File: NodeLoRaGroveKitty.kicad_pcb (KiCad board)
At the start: 2 copper layers, 45 x 50 mm, 40 parts, among them P1 PICKIT PROGRAMMER, P2 Battery, P3 A0, P4 D9, P5 USB-Serial, P6 I2C, SW1 SW_BOOT, SW2 SW_RESET, U1 AP2112, U2 MCP73831T-2ATI/OT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

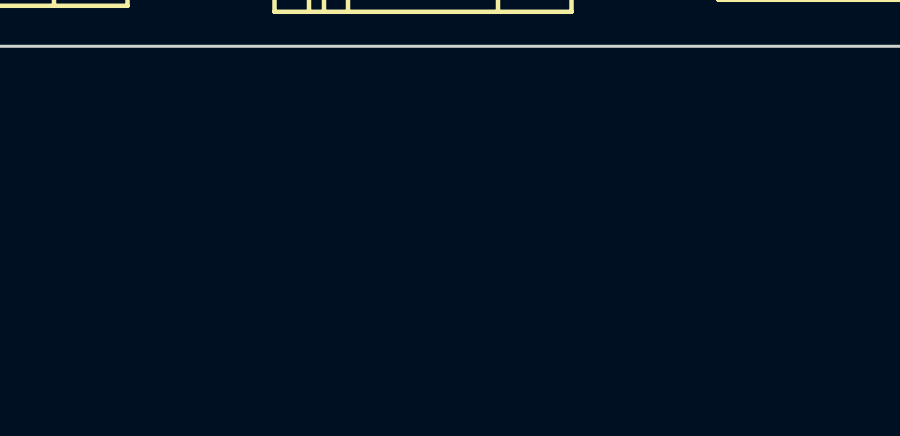
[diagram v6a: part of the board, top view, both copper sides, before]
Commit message: Add resistence and pin reset
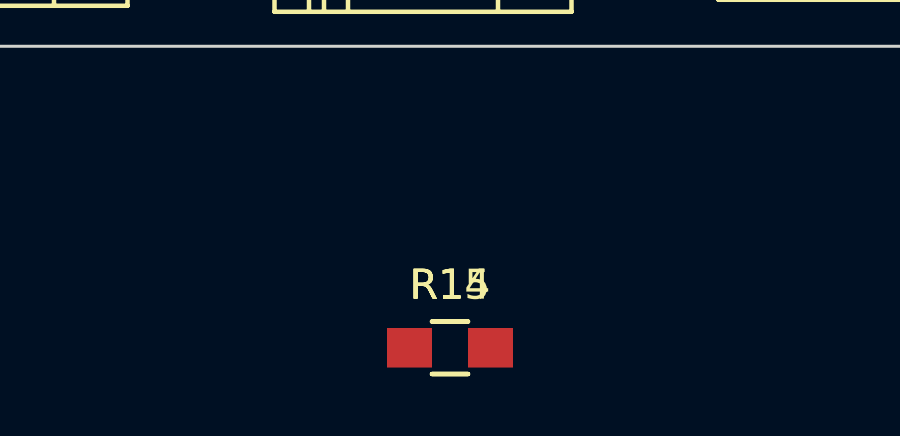
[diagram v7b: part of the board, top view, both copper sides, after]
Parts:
- added R14: 100K, Resistors_SMD:R_0805_HandSoldering, F.Cu at (124.5, 157.1)
- added R15: 10K, Resistors_SMD:R_0805_HandSoldering, F.Cu at (124.5, 157.1)
- R10: value 1K2 -> 100K
- R8: value 330R -> 100K
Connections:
- P3 pad 2: VCC -> +3V3
- P4 pad 2: VCC -> +3V3
- P4 pad 4: /GPIO15 -> /GPIO2
- P6 pad 2: VCC -> +3V3
- R10 pad 1: /A0 -> Net-(R10-Pad1)
- U3 pad 4: /GPIO16 -> /RST_RN
- U3 pad 5: /S_TX/GPIO14 -> /S_TX
- U3 pad 6: /S_RX/GPIO12 -> /S_RX
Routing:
- net VCC: track 136.8 -> 43.1 mm
- net Net-(MODULE1-Pad36): track 42.2 -> 95.3 mm
- net Net-(A1-Pad1): track 25.2 -> 45.5 mm
- net /GPIO2: track 0.00 -> 19.5 mm
- net /GPIO15: track 46.2 -> 26.7 mm
- net /A0: track 37.7 -> 19.4 mm
- net Net-(R10-Pad1): track 0.00 -> 18.3 mm
- net GND: track 68.8 -> 83.5 mm, vias 9 -> 10
- net /S_RX/GPIO12: track 22.6 -> 9.76 mm, vias 1 -> 0
- net /S_RX: track 0.00 -> 12.9 mm, vias 0 -> 1
- net /S_TX: track 0.00 -> 10.5 mm, vias 0 -> 1
- net /S_TX/GPIO14: track 16.2 -> 5.72 mm, vias 1 -> 0
- net +3V3: track 165.7 -> 171.4 mm, vias 3 -> 2

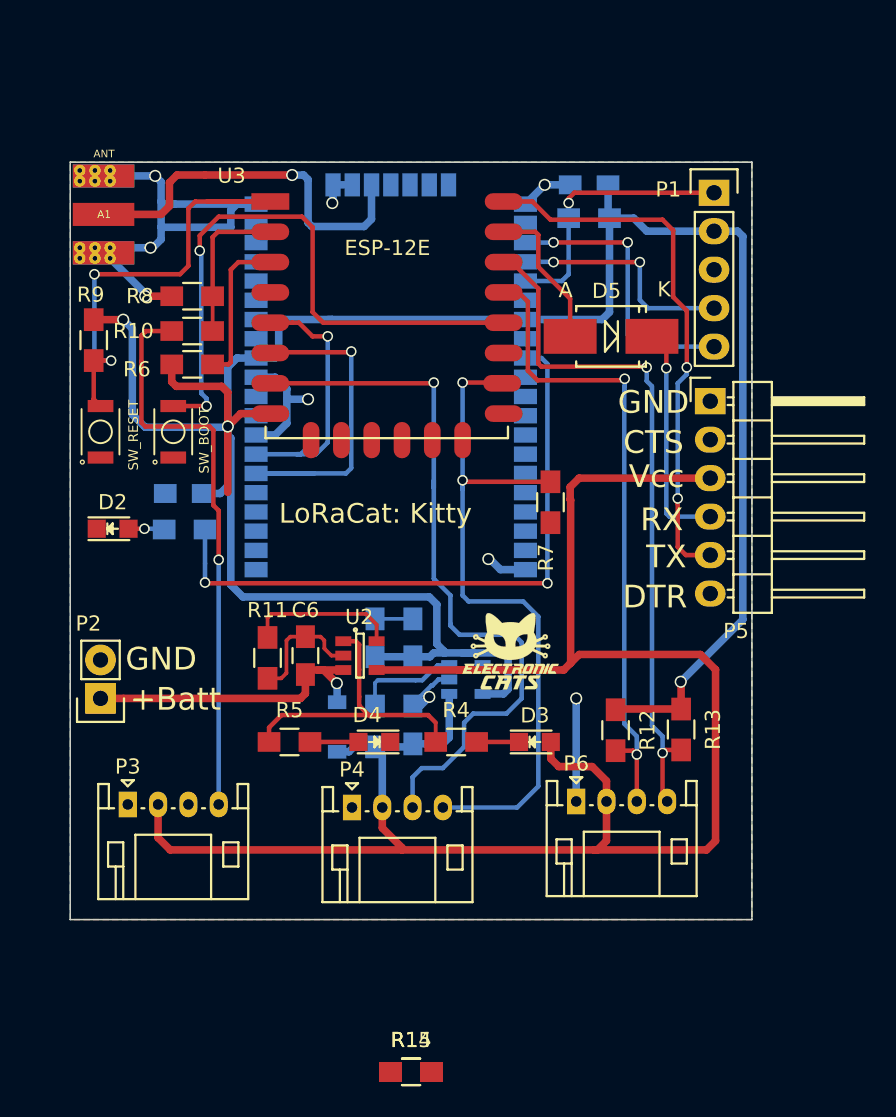
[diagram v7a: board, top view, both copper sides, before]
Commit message: Add res and rst pin PCB and Label's
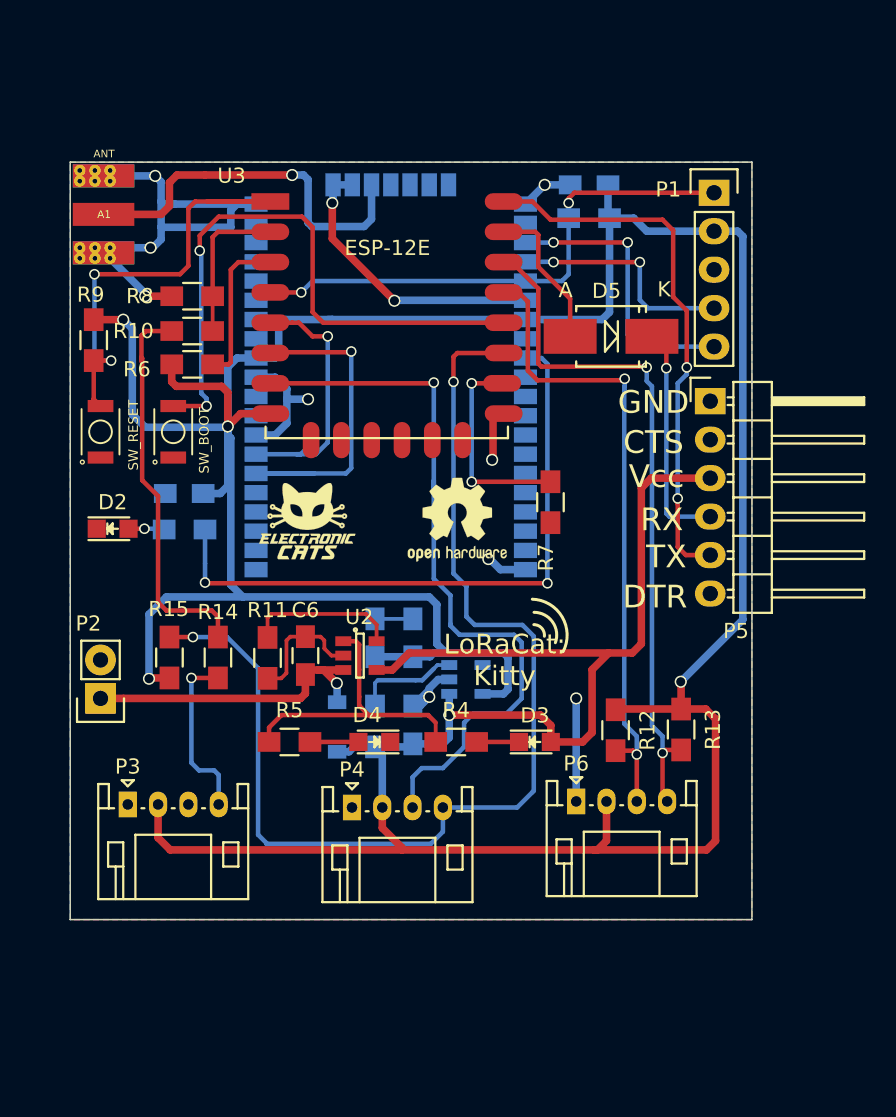
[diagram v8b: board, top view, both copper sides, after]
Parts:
- REF***: moved to F.Cu
- moved R15 31.7 mm to (108.5, 129.7), turned to 90 degrees
- moved R14 30.2 mm to (111.8, 129.7), turned to 90 degrees
- moved REF*** 21.8 mm to (135.0, 130.1)
- moved G*** 15.9 mm to (117.7, 120.7)
- moved REF*** 12.1 mm to (127.5, 120.6), turned to 0 degrees
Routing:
- net +3V3: track 171.4 -> 230.8 mm, vias 2 -> 4
- net /GPIO2: track 19.5 -> 74.0 mm, vias 0 -> 2
- net Net-(MODULE1-Pad36): track 95.3 -> 42.2 mm
- net VCC: track 43.1 -> 64.9 mm, vias 0 -> 1
- net Net-(A1-Pad1): track 45.5 -> 25.2 mm
- net /RST_RN: track 17.8 -> 34.2 mm, vias 1 -> 2
- net /GPIO15: track 26.7 -> 13.2 mm
- net /S_RX/GPIO12: track 9.76 -> 18.0 mm, vias 0 -> 1
- net /S_RX: track 12.9 -> 4.61 mm, vias 1 -> 0
- net /S_TX/GPIO14: track 5.72 -> 13.7 mm, vias 0 -> 1
- net /S_TX: track 10.5 -> 2.46 mm, vias 1 -> 0
- net /A0: track 19.4 -> 11.4 mm
- net Net-(R10-Pad1): track 18.3 -> 26.1 mm
- net GND: track 83.5 -> 90.9 mm, vias 10 -> 11
